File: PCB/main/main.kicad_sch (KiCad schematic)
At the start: 4 parts, among them J1 Conn_01x33_Female, J2 Conn_01x33_Female, J3 Conn_01x33_Female, J4 Conn_01x33_Female

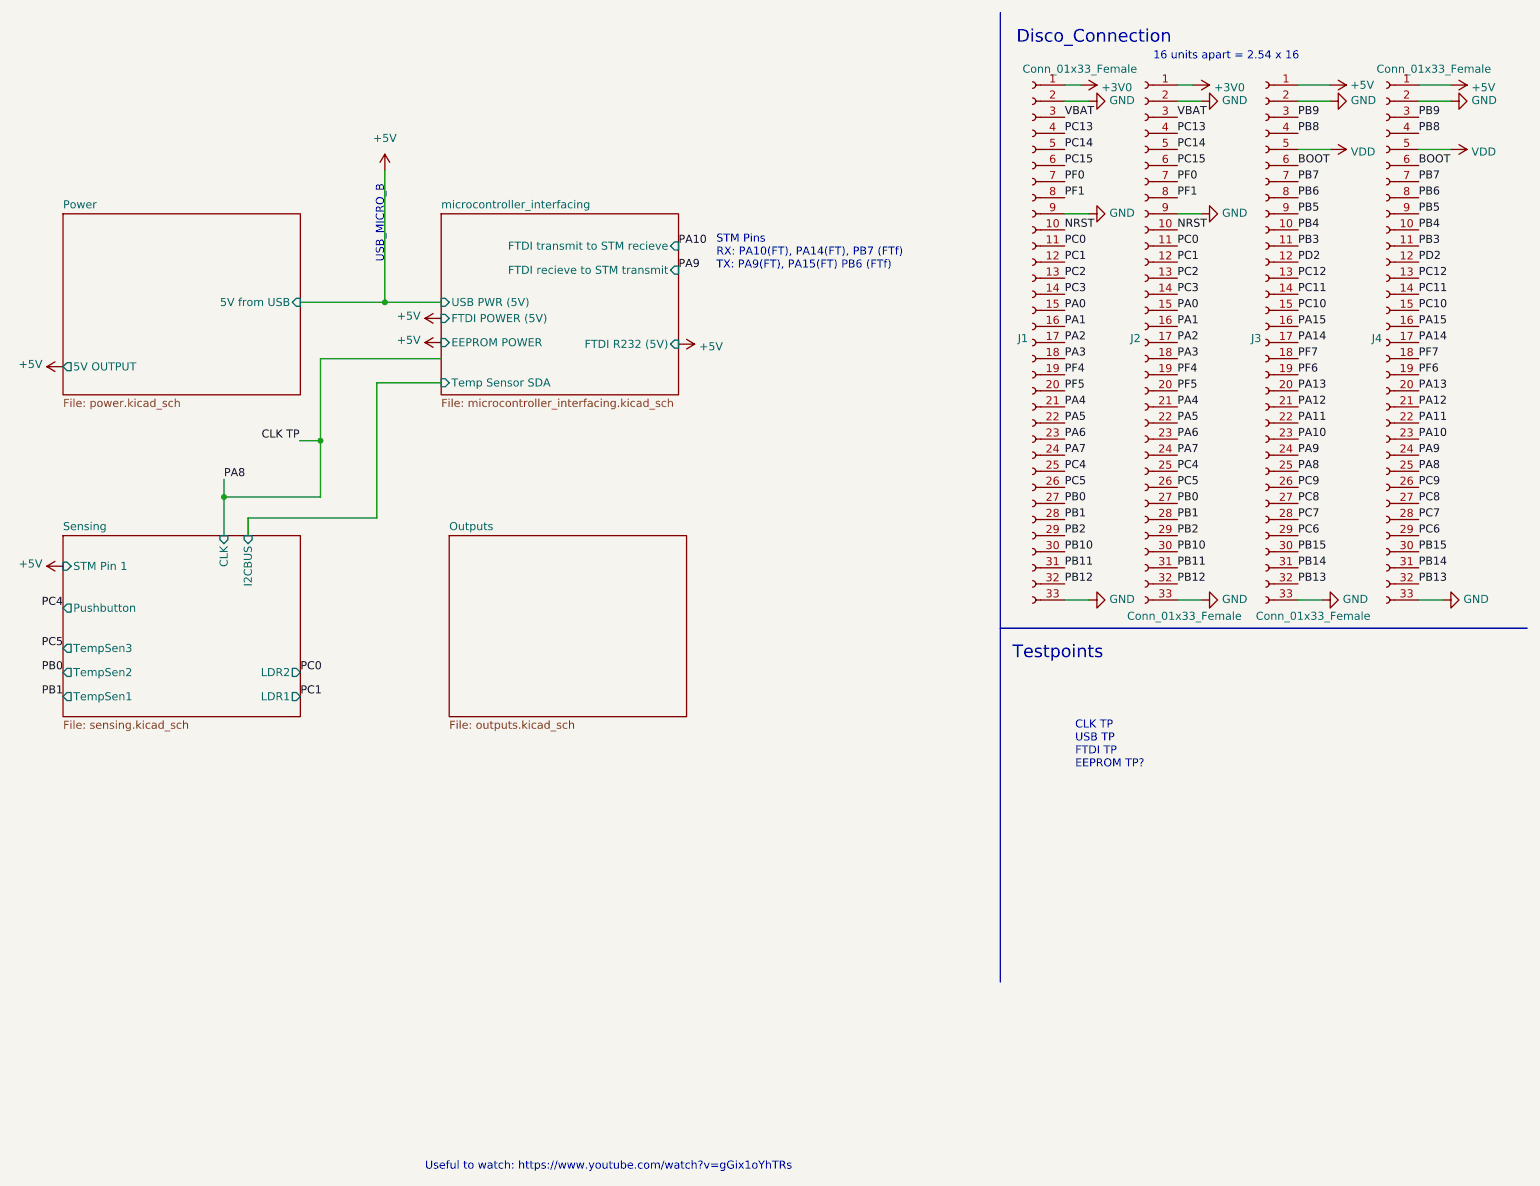
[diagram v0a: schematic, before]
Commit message: updated microcontroller schematic and added documentation
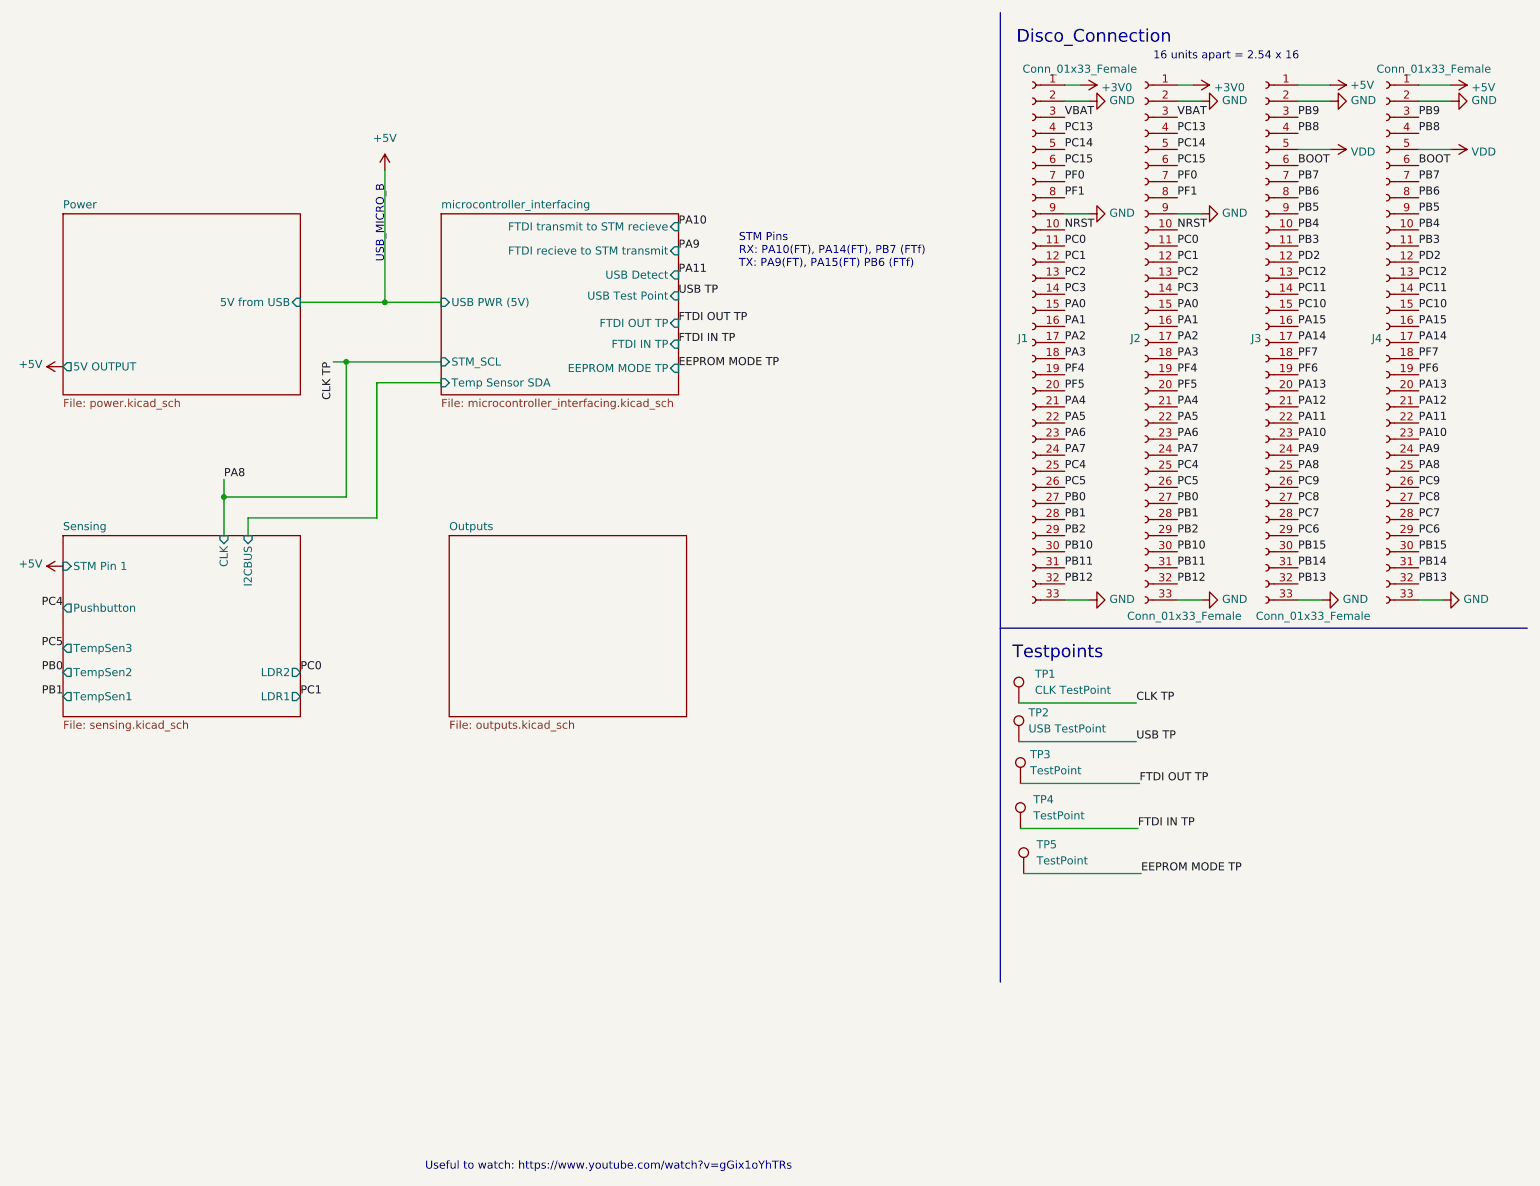
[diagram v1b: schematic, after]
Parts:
- added TP1: CLK TestPoint, symbol Connector:TestPoint
- added TP2: USB TestPoint, symbol Connector:TestPoint
- added TP3, TP4, TP5: TestPoint, symbol Connector:TestPoint
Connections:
- net CLK TP: now also TP1.1
- new net EEPROM MODE TP: TP5.1
- new net FTDI IN TP: TP4.1
- new net FTDI OUT TP: TP3.1
- new net USB TP: TP2.1
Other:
- sheet microcontroller_interfacing ports: added EEPROM MODE TP, FTDI IN TP, FTDI OUT TP, STM_SCL, USB Detect, USB Test Point; removed EEPROM POWER, FTDI POWER (5V), FTDI R232 (5V)
- note removed: "CLK TP USB TP FTDI TP EEPROM TP?"

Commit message: Replace main.kicad_sch
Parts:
- TP1, TP2, TP3, TP4, TP5: footprint (none) -> TestPoint:TestPoint_2Pads_Pitch2.54mm_Drill0.8mm
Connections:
- net CLK TP: no longer J3.25 (Pin_25), J4.25 (Pin_25)
- new net PA8: J3.25 (Pin_25), J4.25 (Pin_25)
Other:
- sheet Power ports: added Output; removed 5V OUTPUT
- sheet Sensing ports: added 5V input; removed Pushbutton , STM Pin 1
- sheet microcontroller_interfacing ports: added none; removed EEPROM MODE TP, FTDI IN TP, FTDI OUT TP, USB Test Point
- note added: "CLK TP"

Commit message: updated microcontroller submodule
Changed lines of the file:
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@@
-    (stroke (width 0) (type default) (color 0 0 0 0))
-  )
-  (wire (pts (xy 49.8094 68.7832) (xy 49.8094 68.58))
     (stroke (width 0) (type default) (color 0 0 0 0))
   )
@@
     (stroke (width 0) (type default) (color 0 0 0 0))
   )
-  (wire (pts (xy 49.8094 68.58) (xy 48.5902 68.58))
+  (wire (pts (xy 48.5648 68.834) (xy 53.34 68.834))
     (stroke (width 0) (type default) (color 0 0 0 0))
   )
@@
     (stroke (width 0) (type default) (color 0 0 0 0))
   )
-  (wire (pts (xy 48.5902 68.58) (xy 48.5902 100.076))
-    (stroke (width 0) (type default) (color 0 0 0 0))
-  )
-  (wire (pts (xy 53.34 68.7832) (xy 49.8094 68.7832))
+  (wire (pts (xy 48.5648 68.834) (xy 48.5902 100.076))
     (stroke (width 0) (type default) (color 0 0 0 0))
   )
@@
       (effects (font (size 1.27 1.27)) (justify right))
     )
-    (pin "Output" input (at 53.34 68.7832 180)
+    (pin "Output" output (at 53.34 68.834 180)
       (effects (font (size 1.27 1.27)) (justify left))
     )
@@
       (reference "R18") (unit 1) (value "4K7") (footprint "Resistor_SMD:R_0201_0603Metric")
     )
+    (path "/59b42903-2dc7-4011-ab5b-d7b81bd233c3/96763a51-1ff4-43a2-9943-9546ef8a9b30"
+      (reference "R19") (unit 1) (value "0") (footprint "Resistor_SMD:R_0201_0603Metric")
+    )
+    (path "/59b42903-2dc7-4011-ab5b-d7b81bd233c3/7f0b7a33-2a31-4936-ad80-c56d49591622"
+      (reference "R20") (unit 1) (value "0") (footprint "Resistor_SMD:R_0201_0603Metric")
+    )
     (path "/59b42903-2dc7-4011-ab5b-d7b81bd233c3/ead29cac-b026-47a5-966a-8205558ed08d"

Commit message: updated gerbers and finalized PCB
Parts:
- J2, J3: Alt_LCSC C12345 (example) -> (none); LCSC C1234 (example) -> (none)
- TP1, TP2, TP3, TP4, TP5: Populate (none) -> DNP
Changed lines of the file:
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@@
+      (effects (font (size 1.27 1.27)) hide)
+    )
+    (property "Populate" "DNP" (id 4) (at 204.978 148.59 0)
       (effects (font (size 1.27 1.27)) hide)
     )
@@
       (effects (font (size 1.27 1.27)) hide)
     )
+    (property "Populate" "DNP" (id 4) (at 204.47 134.366 0)
+      (effects (font (size 1.27 1.27)) hide)
+    )
     (pin "1")
   )
@@
       (effects (font (size 1.27 1.27)) hide)
     )
+    (property "Populate" "DNP" (id 4) (at 204.47 141.478 0)
+      (effects (font (size 1.27 1.27)) hide)
+    )
     (pin "1")
   )
@@
       (effects (font (size 1.27 1.27)) hide)
     )
-    (property "LCSC" "C1234 (example)" (id 4) (at 224.155 64.77 0)
+    (property "LCSC" "" (id 4) (at 224.155 64.77 0)
       (effects (font (size 1.27 1.27)) hide)
     )
@@
       (effects (font (size 1.27 1.27)) hide)
     )
-    (property "Alt_LCSC" "C12345 (example)" (id 6) (at 224.155 64.77 0)
+    (property "Alt_LCSC" "" (id 6) (at 224.155 64.77 0)
       (effects (font (size 1.27 1.27)) hide)
     )
@@
       (effects (font (size 1.27 1.27)) hide)
     )
+    (property "Populate" "DNP" (id 4) (at 204.216 127.762 0)
+      (effects (font (size 1.27 1.27)) hide)
+    )
     (pin "1")
   )
@@
       (effects (font (size 1.27 1.27)) hide)
     )
-    (property "LCSC" "C1234 (example)" (id 4) (at 243.205 64.77 0)
+    (property "LCSC" "" (id 4) (at 243.205 64.77 0)
       (effects (font (size 1.27 1.27)) hide)
     )
@@
       (effects (font (size 1.27 1.27)) hide)
     )
-    (property "Alt_LCSC" "C12345 (example)" (id 6) (at 243.205 64.77 0)
+    (property "Alt_LCSC" "" (id 6) (at 243.205 64.77 0)
       (effects (font (size 1.27 1.27)) hide)
     )
@@
       (effects (font (size 1.27 1.27)) hide)
     )
+    (property "Populate" "DNP" (id 4) (at 204.216 121.666 0)
+      (effects (font (size 1.27 1.27)) hide)
+    )
     (pin "1")
   )
@@
     )
     (path "/59b42903-2dc7-4011-ab5b-d7b81bd233c3/c322890e-14c1-46f5-b267-f55221ee900f"
-      (reference "C4") (unit 1) (value "CT41G-0402-2X1-16V-0.1μF-K(N)") (footprint "Capacitor_SMD:C_0201_0603Metric")
+      (reference "C4") (unit 1) (value "0.1μF") (footprint "Capacitor_SMD:C_0201_0603Metric")
     )
     (path "/d15c8919-7ccc-44b2-8fc4-b04c1b47b6fa/7312d6c1-286a-4148-a5c3-52b226791586"
@@
     )
     (path "/d15c8919-7ccc-44b2-8fc4-b04c1b47b6fa/2cb653ae-a486-4999-8f63-2cc2ca83bff5"
-      (reference "L1") (unit 1) (value "MLP2012V4R7MT0S1") (footprint "Inductor_SMD:L_0805_2012Metric")
+      (reference "L1") (unit 1) (value "MLP2012V4R7MT0S1") (footprint "3088HAT:INDC2012X87N")
     )
     (path "/cf6c12a4-3d95-473d-bafe-8be3892a84e9/90369ffc-d873-4b5f-ab01-ddf820143b6f"
@@
     )
     (path "/d15c8919-7ccc-44b2-8fc4-b04c1b47b6fa/768374ff-fcd3-47db-8a39-62497a662f1b"
-      (reference "R1") (unit 1) (value "1650") (footprint "Resistor_SMD:R_0201_0603Metric")
+      (reference "R1") (unit 1) (value "1800") (footprint "Resistor_SMD:R_0201_0603Metric")
     )
     (path "/d15c8919-7ccc-44b2-8fc4-b04c1b47b6fa/625263f4-7654-4012-90f5-ccfddd1120cf"
@@
     )
     (path "/d15c8919-7ccc-44b2-8fc4-b04c1b47b6fa/ced83566-388d-4f99-be31-41bdc857545a"
-      (reference "R3") (unit 1) (value "100") (footprint "Resistor_SMD:R_0201_0603Metric")
+      (reference "R3") (unit 1) (value "100ohms") (footprint "Resistor_SMD:R_0201_0603Metric")
     )
     (path "/d15c8919-7ccc-44b2-8fc4-b04c1b47b6fa/a6859af7-c2bb-496d-bf21-a4a555131e66"
@@
     )
     (path "/d15c8919-7ccc-44b2-8fc4-b04c1b47b6fa/842d48ad-8b90-46f9-8160-46c5ec76f179"
-      (reference "R5") (unit 1) (value "1000") (footprint "Resistor_SMD:R_0201_0603Metric")
+      (reference "R5") (unit 1) (value "1200") (footprint "Resistor_SMD:R_0201_0603Metric")
     )
     (path "/d15c8919-7ccc-44b2-8fc4-b04c1b47b6fa/6fe27d7a-8728-4218-b48e-6f66377c607f"
